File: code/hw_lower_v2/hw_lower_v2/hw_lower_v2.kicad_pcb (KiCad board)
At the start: 4 copper layers, 102 x 104.8 mm, 115 parts, among them J1 Screw_Terminal_01x01, J14 Conn_01x02, J2 Screw_Terminal_01x01, J3 Screw_Terminal_01x01, J4 Screw_Terminal_01x01, J5 Screw_Terminal_01x01, J6 Screw_Terminal_01x01, J7 Conn_01x06_Pin, J8 Conn_02x20_Odd_Even, K1 AHES4191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

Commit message: right before tracks
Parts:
- moved J14 90.2 mm to (103.5, 187.5)
- moved J1 16.5 mm to (196.5, 113.8)
- moved J5 16.2 mm to (104.8, 113.0), turned to 180 degrees
- moved J6 15.8 mm to (118.8, 105.2), turned to -90 degrees
- moved J2 15.0 mm to (183.2, 106.2)
- moved C21 7.63 mm to (139.9, 170.2), turned to 90 degrees
- moved JP3 6.77 mm to (131.2, 174.2)
- moved C15 6.72 mm to (135.4, 162.9), turned to 180 degrees
- moved C16 6.50 mm to (130.9, 169.4), turned to -90 degrees
- moved D8 5.69 mm to (131.2, 177.8), turned to 180 degrees
- moved R5 4.75 mm to (139.8, 198.3), turned to -90 degrees
- moved R1 4.68 mm to (135.2, 198.3), turned to -90 degrees
- moved R3 3.48 mm to (137.5, 198.3), turned to -90 degrees
- moved R6 3.32 mm to (139.8, 201.3), turned to -90 degrees
- moved R2 3.22 mm to (135.2, 201.3), turned to -90 degrees
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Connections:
- K1 pad 5: /AC/N_internal_power -> /AC/L_internal_power
- K1 pad 6: /AC/N_out -> /AC/L_out
- K1 pad 7: /AC/L_internal_power -> /AC/N_internal_power
- K1 pad 8: /AC/L_out -> /AC/N_out
- R10 pad 2: /AC/N_internal_power -> /AC/L_internal_power
- R9 pad 1: /AC/L_internal_power -> /AC/N_internal_power
- U1 pad 10: /AC/N_in -> /AC/L_in
- U1 pad 11: /AC/N_internal_power -> /AC/L_internal_power
- U1 pad 8: /AC/L_in -> /AC/N_in
- U1 pad 9: /AC/L_internal_power -> /AC/N_internal_power
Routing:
- added copper zone on In2.Cu, net +12V
- added copper zone on In2.Cu, net +3.3V
- added copper zone on In2.Cu, net +5V
- added copper zone on F.Cu, net Net-(JP4-B)
- removed copper zone on F.Cu, net +3.3V
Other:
- board text added: "${CURRENT_DATE}"
- board text added: "BlueEVSE"
- board text added: "Version:0.1"

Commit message: routed most of the board
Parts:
- moved R15 10.2 mm to (112.5, 160.2), turned to 180 degrees
- moved R24 10.0 mm to (178.7, 195.6)
- moved R26 10.0 mm to (180.2, 195.6)
- moved R17 9.76 mm to (112.5, 161.7)
- moved R44 9.34 mm to (122.1, 178.3), turned to 0 degrees
- moved D8 9.14 mm to (122.1, 176.8), turned to 0 degrees
- moved Q1 8.64 mm to (112.5, 157.4), turned to 90 degrees
- moved C21 7.51 mm to (138.9, 177.6)
- moved JP3 7.18 mm to (125.3, 178.3)
- moved C2 6.53 mm to (120.2, 162.9), turned to 180 degrees
- moved C15 6.46 mm to (134.5, 169.2)
- moved C16 6.46 mm to (130.0, 175.8)
- moved U5 6.46 mm to (135.1, 175.9)
- moved C8 4.60 mm to (128.1, 183.2)
- moved R33 3.98 mm to (119.3, 181.7)
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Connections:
- J8 pad 11: /AC/POWER_MEASUREMENT_INFO -> /AC/GFCI_FAULT
- J8 pad 19: /AC/GFCI_FAULT -> /AC/POWER_MEASUREMENT_INFO
- J8 pad 21: /AC/GFCI_CALIBRATE -> unconnected-(J8-Pin_21-Pad21)
- J8 pad 23: /AC/GFCI_TEST -> unconnected-(J8-Pin_23-Pad23)
- J8 pad 7: unconnected-(J8-Pin_7-Pad7) -> /AC/GFCI_TEST
- J8 pad 9: unconnected-(J8-Pin_9-Pad9) -> /AC/GFCI_CALIBRATE
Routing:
- net /AC/AC_RELAY_SENSE: track 0.00 -> 64.2 mm
- net /AC/AC_RELAY_PWM: track 0.00 -> 62.7 mm, vias 0 -> 1
- net /EVSE control and status/LOCK_SENSE: track 0.00 -> 61.8 mm
- net /EVSE control and status/PROXIMITY_PILOT: track 0.00 -> 54.5 mm
- net Net-(U1-Fault): track 0.00 -> 48.4 mm, vias 0 -> 2
- net /EVSE control and status/CONTROL_PILOT_SENSE: track 0.00 -> 46.6 mm
- net /AC/GFCI_TEST: track 0.00 -> 44.1 mm, vias 0 -> 1
- net /AC/GFCI_CALIBRATE: track 0.00 -> 42.3 mm, vias 0 -> 1
- net /EVSE control and status/CONTROL_PILOT_PWM: track 0.00 -> 42.1 mm
- net +12V: track 0.00 -> 41.3 mm, vias 0 -> 14
- net /EVSE control and status/LOCK_B: track 0.00 -> 39.8 mm, vias 0 -> 2
- net /AC/POWER_MEASUREMENT_CLK: track 0.00 -> 39.3 mm
- net /AC/N_internal_power: track 0.00 -> 38.4 mm, vias 0 -> 20
- net /EVSE control and status/LOCK_A: track 0.00 -> 37.7 mm, vias 0 -> 2
- net /AC/POWER_MEASUREMENT_RX: track 0.00 -> 34.5 mm
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- added copper zone on B.Cu, net /AC/L_in
- added copper zone on F.Cu, net /AC/L_in
- added copper zone on In1.Cu, net /AC/L_in
- added copper zone on In2.Cu, net /AC/L_in
- added copper zone on B.Cu, net /AC/L_internal_power
- added copper zone on F.Cu, net /AC/L_internal_power
- added copper zone on In1.Cu, net /AC/L_internal_power
- added copper zone on In2.Cu, net /AC/L_internal_power
- added copper zone on B.Cu, net /AC/L_out
- added copper zone on F.Cu, net /AC/L_out
- added copper zone on In1.Cu, net /AC/L_out
- added copper zone on In2.Cu, net /AC/L_out
- added copper zone on B.Cu, net /AC/N_in
- added copper zone on F.Cu, net /AC/N_in
- added copper zone on In1.Cu, net /AC/N_in
- added copper zone on B.Cu, net /AC/N_internal_power
- added copper zone on F.Cu, net /AC/N_internal_power
- added copper zone on In1.Cu, net /AC/N_internal_power
- added copper zone on In2.Cu, net /AC/N_internal_power
- added copper zone on B.Cu, net /AC/N_out
- added copper zone on F.Cu, net /AC/N_out
- added copper zone on In1.Cu, net /AC/N_out
- added copper zone on In2.Cu, net /AC/N_out
- added copper zone on B.Cu, net Earth_Protective
- added copper zone on F.Cu, net Earth_Protective
- added copper zone on In1.Cu, net Earth_Protective
- added copper zone on In2.Cu, net Earth_Protective
- added copper zone on F.Cu, net GND

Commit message: before the final route
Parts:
- moved C20 10.1 mm to (188.3, 182.4), turned to 180 degrees
- moved C17 9.18 mm to (142.1, 168.4), turned to 180 degrees
- moved R42 8.09 mm to (151.4, 180.7), turned to 180 degrees
- moved C19 7.50 mm to (142.1, 176.7)
- moved C18 6.46 mm to (188.0, 175.3)
- moved R40 6.46 mm to (195.8, 170.3)
- moved R41 6.46 mm to (195.8, 168.8)
- moved U7 6.46 mm to (194.5, 175.8)
- moved R38 6.33 mm to (150.3, 166.4)
- moved R39 6.33 mm to (150.3, 164.9)
- moved U6 6.33 mm to (149.3, 171.7)
- moved C15 5.21 mm to (132.3, 164.5)
- moved U5 5.21 mm to (132.9, 171.2)
- moved C16 5.21 mm to (127.8, 171.0)
- moved C21 5.21 mm to (136.7, 172.9)
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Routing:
- net /AC/AC_RELAY_SENSE: track 64.2 -> 0.00 mm
- net /AC/AC_RELAY_PWM: track 62.7 -> 0.00 mm, vias 1 -> 0
- net /EVSE control and status/LOCK_SENSE: track 61.8 -> 0.00 mm
- net /EVSE control and status/PROXIMITY_PILOT: track 54.5 -> 0.00 mm
- net Net-(U1-Fault): track 48.4 -> 0.00 mm, vias 2 -> 0
- net /EVSE control and status/CONTROL_PILOT_SENSE: track 46.6 -> 0.00 mm
- net /AC/GFCI_TEST: track 44.1 -> 0.00 mm, vias 1 -> 0
- net /AC/GFCI_CALIBRATE: track 42.3 -> 0.00 mm, vias 1 -> 0
- net /EVSE control and status/CONTROL_PILOT_PWM: track 42.1 -> 0.00 mm
- net +12V: track 41.3 -> 0.00 mm, vias 14 -> 0
- net /EVSE control and status/LOCK_B: track 39.8 -> 0.00 mm, vias 2 -> 0
- net /AC/POWER_MEASUREMENT_CLK: track 39.3 -> 0.00 mm
- net /AC/N_internal_power: track 38.4 -> 0.00 mm, vias 20 -> 0
- net /EVSE control and status/LOCK_A: track 37.7 -> 0.00 mm, vias 2 -> 0
- net /AC/POWER_MEASUREMENT_RX: track 34.5 -> 0.00 mm
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- added copper zone on B.Cu, net GND
- removed copper zone on F.Cu, net GND

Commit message: layout 99% finished
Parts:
- moved JP4 16.2 mm to (139.5, 184.4), turned to 90 degrees
- moved D5 12.7 mm to (142.5, 185.0), turned to 180 degrees
- moved R41 12.5 mm to (196.2, 181.2), turned to 180 degrees
- moved R40 11.3 mm to (192.9, 181.2)
- moved R39 11.1 mm to (150.5, 176.0), turned to 180 degrees
- moved R38 10.1 mm to (147.2, 176.0)
- moved C18 9.12 mm to (195.8, 170.5), turned to 0 degrees
- moved C17 8.78 mm to (150.2, 165.2), turned to 0 degrees
- moved C19 7.47 mm to (148.4, 180.5), turned to 0 degrees
- moved R42 7.30 mm to (145.5, 185.0), turned to 0 degrees
- moved C20 6.59 mm to (194.0, 185.8), turned to 0 degrees
- moved JP5 5.50 mm to (186.3, 189.6)
- moved R43 5.32 mm to (192.6, 190.2)
- moved U6 3.02 mm to (146.3, 171.3), turned to 0 degrees
- moved U7 2.84 mm to (191.8, 176.5), turned to 0 degrees
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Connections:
- J8 pad 1: +12V -> unconnected-(J8-Pin_1-Pad1)
- J8 pad 21: unconnected-(J8-Pin_21-Pad21) -> +12V
- J8 pad 23: unconnected-(J8-Pin_23-Pad23) -> +12V
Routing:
- net +12V: track 0.00 -> 113.2 mm, vias 0 -> 17
- net /AC/AC_RELAY_PWM: track 0.00 -> 64.1 mm, vias 0 -> 1
- net /AC/AC_RELAY_SENSE: track 0.00 -> 63.0 mm
- net /EVSE control and status/LOCK_SENSE: track 0.00 -> 61.6 mm
- net /EVSE control and status/PROXIMITY_PILOT: track 0.00 -> 56.8 mm
- net Net-(U1-Fault): track 0.00 -> 48.0 mm, vias 0 -> 2
- net /EVSE control and status/LOCK_B: track 0.00 -> 46.3 mm, vias 0 -> 2
- net /EVSE control and status/LOCK_A: track 0.00 -> 43.0 mm, vias 0 -> 2
- net /EVSE control and status/CONTROL_PILOT_SENSE: track 0.00 -> 42.6 mm, vias 0 -> 1
- net /AC/GFCI_TEST: track 0.00 -> 41.1 mm, vias 0 -> 1
- net /AC/GFCI_CALIBRATE: track 0.00 -> 40.8 mm, vias 0 -> 1
- net /AC/POWER_MEASUREMENT_CLK: track 0.00 -> 37.9 mm, vias 0 -> 1
- net /EVSE control and status/CONTROL_PILOT_PWM: track 0.00 -> 37.6 mm, vias 0 -> 1
- net /AC/POWER_MEASUREMENT_RX: track 0.00 -> 35.0 mm, vias 0 -> 1
- net /AC/POWER_MEASUREMENT_TX: track 0.00 -> 32.8 mm, vias 0 -> 1
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- added copper zone on F.Cu, net GND
- added copper zone on F.Cu, net Net-(JP5-B)
- removed copper zone on B.Cu, net GND
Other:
- board text added: "+12V"
- board text added: "+3V3"
- board text added: "+5V"
- board text added: "-12V"
- board text added: "GND"
- board text added: "Lovro Oreskovic"
- board text added: "Vin"

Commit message: wip
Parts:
- moved R7 0.55 mm to (159.2, 132.5)
- moved R8 0.55 mm to (159.2, 127.7)
- moved R9 0.55 mm to (159.2, 123.0)
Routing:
- net /AC/N_internal_power: track 28.7 -> 29.2 mm
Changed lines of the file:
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@@
 	(footprint "Resistor_SMD:R_1206_3216Metric"
 		(layer "F.Cu")
-		(at 159.75 122.9625 -90)
+		(at 159.2 122.9625 -90)
 		(descr "Resistor SMD 1206 (3216 Metric), square (rectangular) end terminal, IPC_7351 nominal, (Body size source: IPC-SM-782 page 72, https://www.pcb-3d.com/wordpress/wp-content/uploads/ipc-sm-782a_amendment_1_and_2.pdf), generated with kicad-footprint-generator")
 		(tags "resistor")
@@
 	(footprint "Resistor_SMD:R_1206_3216Metric"
 		(layer "F.Cu")
-		(at 159.75 127.7125 -90)
+		(at 159.2 127.7125 -90)
 		(descr "Resistor SMD 1206 (3216 Metric), square (rectangular) end terminal, IPC_7351 nominal, (Body size source: IPC-SM-782 page 72, https://www.pcb-3d.com/wordpress/wp-content/uploads/ipc-sm-782a_amendment_1_and_2.pdf), generated with kicad-footprint-generator")
 		(tags "resistor")
@@
 		(sheetname "Root")
 		(sheetfile "hw_lower_v2.kicad_sch")
-		(attr smd exclude_from_bom)
+		(attr smd exclude_from_pos_files exclude_from_bom)
 		(fp_circle
 			(center 0 0)
@@
 		(sheetname "Root")
 		(sheetfile "hw_lower_v2.kicad_sch")
-		(attr smd exclude_from_bom)
+		(attr smd exclude_from_pos_files exclude_from_bom)
 		(fp_circle
 			(center 0 0)
@@
 		(sheetname "Root")
 		(sheetfile "hw_lower_v2.kicad_sch")
-		(attr smd exclude_from_bom)
+		(attr smd exclude_from_pos_files exclude_from_bom)
 		(fp_circle
 			(center 0 0)
@@
 		(sheetname "Power supply")
 		(sheetfile "power_supply.kicad_sch")
-		(attr through_hole exclude_from_pos_files)
+		(attr through_hole exclude_from_pos_files exclude_from_bom)
 		(fp_line
 			(start -1.33 -1.33)
@@
 		(tags "Through hole pin header THT 2x20 2.54mm double row")
 		(property "Reference" "J8"
-			(at -2.56 -1.12 180)
+			(at 4.34 -2.92 180)
 			(layer "F.SilkS")
 			(effects
@@
 	(footprint "Resistor_SMD:R_1206_3216Metric"
 		(layer "F.Cu")
-		(at 159.75 132.4625 -90)
+		(at 159.2 132.4625 -90)
 		(descr "Resistor SMD 1206 (3216 Metric), square (rectangular) end terminal, IPC_7351 nominal, (Body size source: IPC-SM-782 page 72, https://www.pcb-3d.com/wordpress/wp-content/uploads/ipc-sm-782a_amendment_1_and_2.pdf), generated with kicad-footprint-generator")
 		(tags "resistor")
@@
 		(sheetname "Root")
 		(sheetfile "hw_lower_v2.kicad_sch")
-		(attr smd exclude_from_bom)
+		(attr smd exclude_from_pos_files exclude_from_bom)
 		(fp_circle
 			(center 0 0)
@@
 		(sheetname "Root")
 		(sheetfile "hw_lower_v2.kicad_sch")
-		(attr smd exclude_from_bom)
+		(attr smd exclude_from_pos_files exclude_from_bom)
 		(fp_circle
 			(center 0 0)
@@
 		(sheetname "Root")
 		(sheetfile "hw_lower_v2.kicad_sch")
-		(attr smd exclude_from_bom)
+		(attr smd exclude_from_pos_files exclude_from_bom)
 		(fp_circle
 			(center 0 0)
@@
 	)
 	(segment
-		(start 159.75 131)
-		(end 159.75 129.175)
+		(start 159.2 131)
+		(end 159.2 129.175)
 		(width 0.3)
 		(layer "F.Cu")
@@
 	)
 	(segment
-		(start 159.75 126.25)
-		(end 159.75 124.425)
+		(start 159.2 126.25)
+		(end 159.2 124.425)
 		(width 0.3)
 		(layer "F.Cu")
@@
 	)
 	(segment
-		(start 160.9 120.65)
-		(end 171.23 120.65)
-		(width 0.3)
-		(layer "F.Cu")
-		(net 56)
-	)
-	(segment
 		(start 128.749873 102.449961)
 		(end 128.749873 109.25)
@@
 	)
 	(segment
-		(start 159.75 121.5)
-		(end 160.05 121.5)
+		(start 159.2 121.5)
+		(end 159.5 121.5)
 		(width 0.3)
 		(layer "F.Cu")
@@
 	)
 	(segment
-		(start 160.05 121.5)
-		(end 160.9 120.65)
+		(start 160.35 120.65)
+		(end 171.23 120.65)
+		(width 0.3)
+		(layer "F.Cu")
+		(net 56)
+	)
+	(segment
+		(start 159.5 121.5)
+		(end 160.35 120.65)
 		(width 0.3)
 		(layer "F.Cu")

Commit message: finish 3d models
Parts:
- C12: footprint multi_new:CAP-TH_L18.0-W7.0-P15.00-D0.7 -> multi_new:CAP-TH_L13.0-W6.0-P10.00-D0.6
- moved R7 9.41 mm to (159.3, 123.0)
- moved R8 8.69 mm to (161.2, 119.2), turned to 180 degrees
- moved R9 7.69 mm to (165.9, 119.2), turned to 180 degrees
- moved F1 5.07 mm to (146.1, 107.6), turned to 90 degrees
- moved RV1 4.39 mm to (137.7, 104.3)
- moved C12 1.79 mm to (137.8, 110.2)
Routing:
- net /AC/N_internal_power: track 29.2 -> 19.2 mm
- net Net-(T1-AB): track 6.07 -> 15.7 mm
- net /AC/L_internal_power: track 25.1 -> 29.6 mm
- net Net-(PS1-AC/L): track 19.0 -> 18.1 mm
- net Net-(R7-Pad1): track 1.82 -> 2.51 mm
- net Net-(U1-CT_S2): vias 1 -> 2
- net GND: vias 4 -> 77
- removed copper zone on In1.Cu, net /AC/L_internal_power
- removed copper zone on In2.Cu, net /AC/L_internal_power
- removed copper zone on In1.Cu, net /AC/N_internal_power
- removed copper zone on In2.Cu, net /AC/N_internal_power

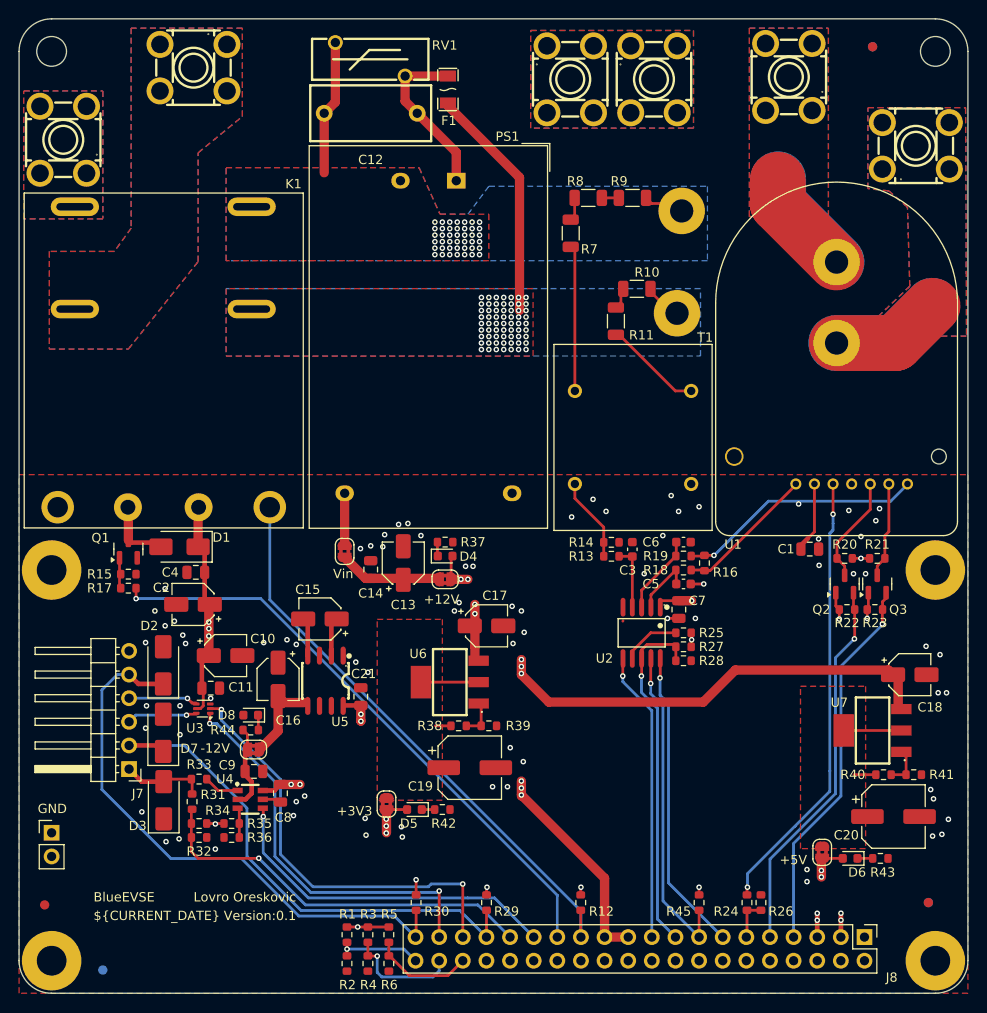
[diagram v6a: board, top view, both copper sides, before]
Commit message: moved stuff around a little bit, will optimise the number of components now
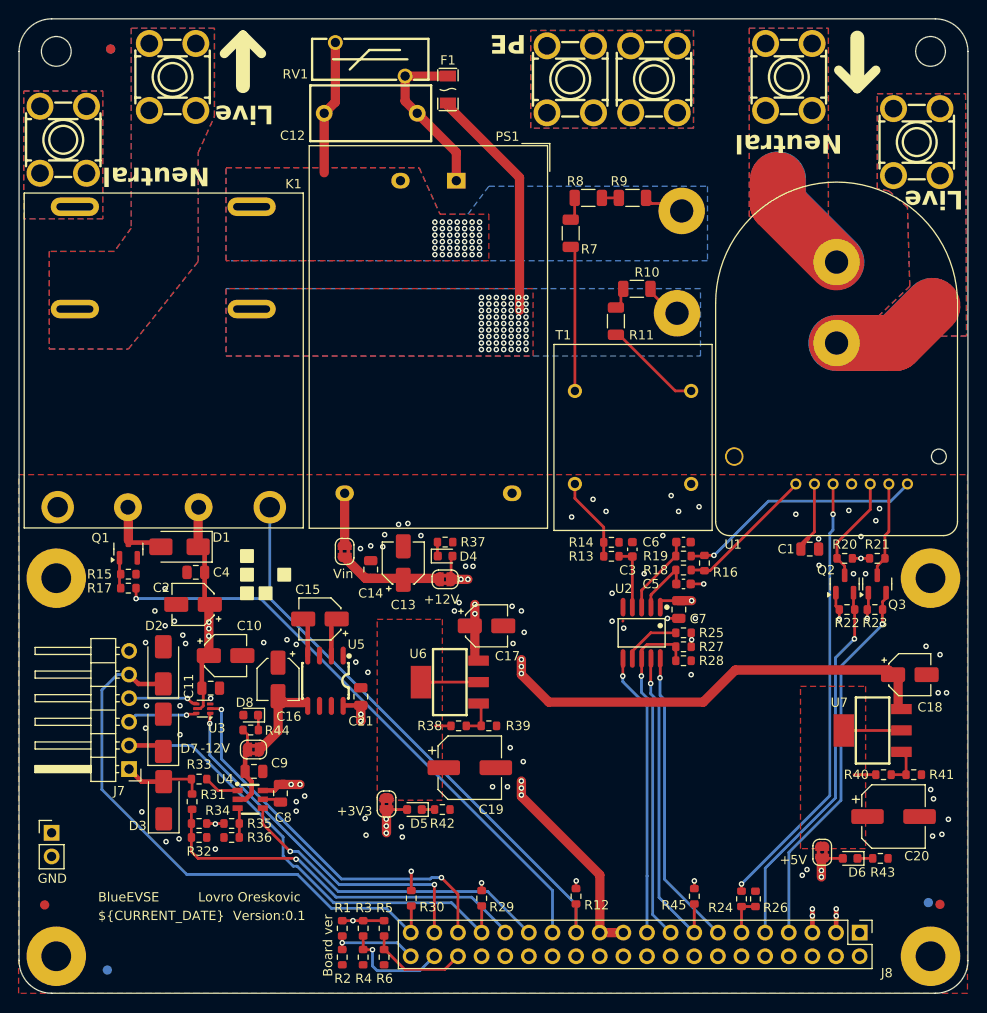
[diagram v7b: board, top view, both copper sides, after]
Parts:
- moved FID2 81.9 mm to (109.8, 103.2)
- moved FID4 81.9 mm to (109.8, 103.2)
- moved J6 2.46 mm to (116.5, 106.2), turned to 0 degrees
- moved FID5 1.26 mm to (199.0, 195.2)
- moved H3 1.02 mm to (198.0, 160.1)
- moved H4 1.01 mm to (104.0, 160.1)
- moved R12 0.85 mm to (159.9, 194.3)
- moved R2 0.85 mm to (134.7, 200.9)
- moved R4 0.85 mm to (137.0, 200.9)
- moved R45 0.85 mm to (172.6, 194.3)
- moved R6 0.85 mm to (139.2, 200.9)
- moved R1 0.85 mm to (134.7, 197.8)
- moved R3 0.85 mm to (137.0, 197.8)
- moved R5 0.85 mm to (139.2, 197.8)
- moved R24 0.71 mm to (177.7, 194.6)
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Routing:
- net /EVSE control and status/LOCK_B: track 46.3 -> 42.3 mm
- net /EVSE control and status/LOCK_A: track 43.0 -> 39.5 mm
- net /EVSE control and status/PROXIMITY_PILOT: track 56.8 -> 54.3 mm
- net /EVSE control and status/CONTROL_PILOT_PWM: track 37.6 -> 35.1 mm
- net /EVSE control and status/CONTROL_PILOT_SENSE: track 42.6 -> 41.7 mm
- net +12V: track 113.2 -> 112.3 mm
- net /EVSE control and status/LOCK_SENSE: track 61.6 -> 60.9 mm
- net /AC/AC_RELAY_SENSE: track 63.0 -> 62.3 mm
- net /AC/POWER_MEASUREMENT_CLK: track 37.9 -> 37.2 mm
- net /AC/POWER_MEASUREMENT_TX: track 32.8 -> 32.1 mm
- net /AC/POWER_MEASUREMENT_INFO: track 31.3 -> 30.6 mm
- net /BV1: track 12.3 -> 11.8 mm
- net Net-(U1-CT_S2): vias 2 -> 1
- net GND: vias 77 -> 82
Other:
- board text added: "1"
- board text added: "Board ver"
- board text added: "Live"
- board text added: "Neutral"
- board text added: "PE"
